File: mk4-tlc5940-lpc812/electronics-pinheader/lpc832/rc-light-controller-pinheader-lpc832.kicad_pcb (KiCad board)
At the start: 2 copper layers, 44 x 23 mm, 14 parts, among them J1 Pinheader right-angle 2x17, J2 Pinheader straight 1x06, J3 Pinheader straight 1x06, T9 PMV30UN, U1 LPC832M101FDH20, U2 TLC5940PWP, U3 MCP1703A-3302_SOT23

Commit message: Streamline gerber filenames and add schematics PDF everywhere
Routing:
- net GND: vias 21 -> 22
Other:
- board text added: "832 Rev2"
- board text added: "Mk4P"
- board text added: "RC Light Controller"
- board text removed: "RC Light Controller Mk4P"
- board text removed: "Rev1"

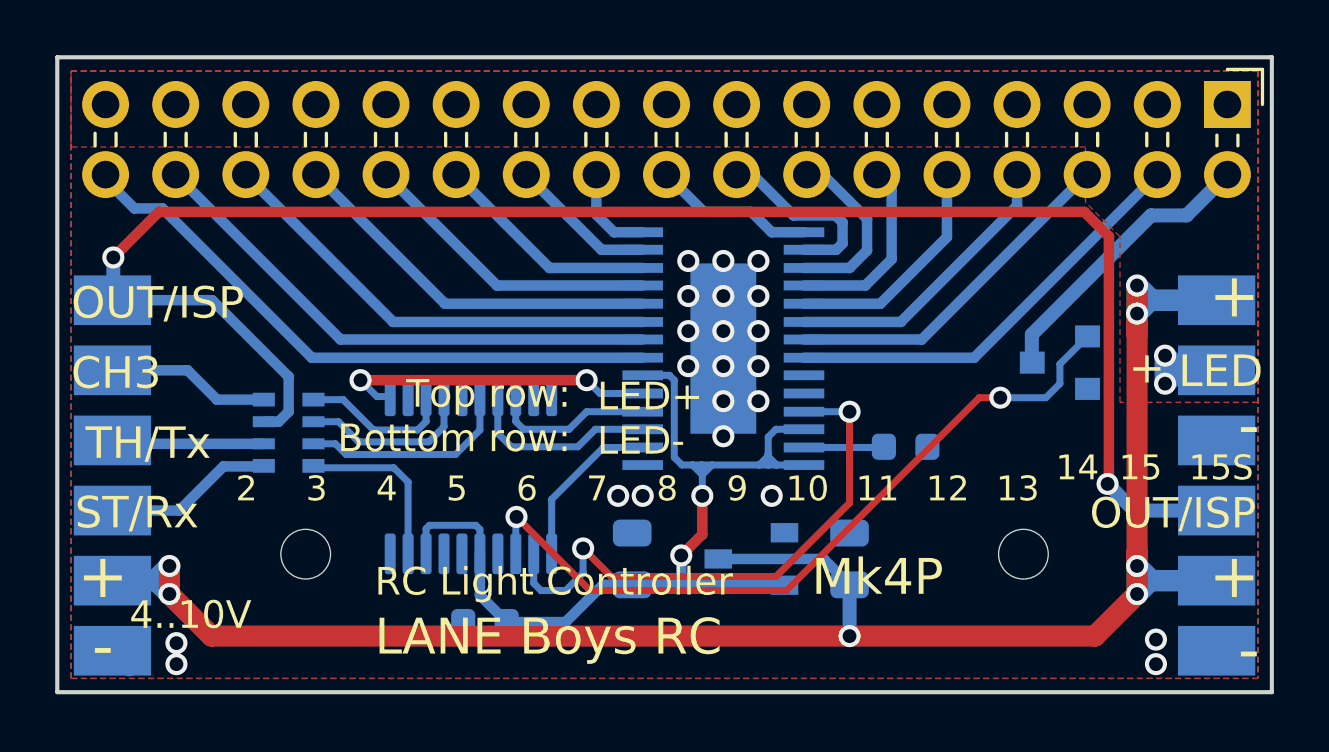
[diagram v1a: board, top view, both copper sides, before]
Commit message: Improve FAB layer and silkscreen
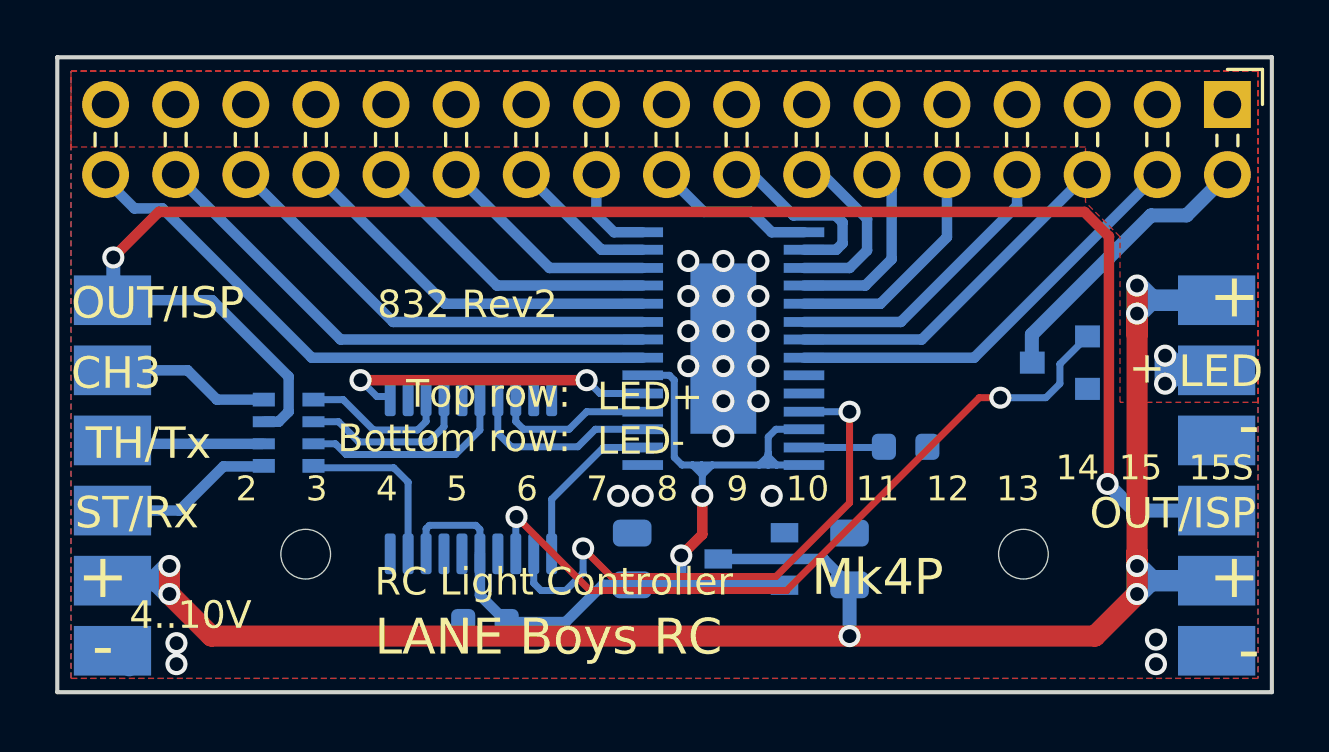
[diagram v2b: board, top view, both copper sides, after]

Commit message: Add Gerber for LPC832 variants
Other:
- rule pad_to_mask_clearance: 0.0254 -> 0
